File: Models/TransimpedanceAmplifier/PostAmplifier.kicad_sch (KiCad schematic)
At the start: 18 parts, among them J10 Conn_01x02_Pin, J8 Conn_01x02_Pin, J9 Conn_01x02_Pin, Q1 Q_PNP, Q2 Q_NPN, U5 OP37G

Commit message: Working on filling in the last details of the schematics
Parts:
- C15, C16: footprint (none) -> TwoTerminal:CAPC0603; Cost (none) -> $0.00; RoHS Compliant (none) -> NO
- D4, D5: footprint (none) -> TwoTerminal:SOD-123; Cost (none) -> $0.00; RoHS Compliant (none) -> NO
- D6, D7: footprint (none) -> ThreeTerminal:SOT-23; Cost (none) -> $0.00; RoHS Compliant (none) -> NO
- J10, J8, J9: footprint (none) -> Connector_Custom:PinHeader_1x2; Cost (none) -> $0.00; RoHS Compliant (none) -> NO
- Q1, Q2, R12, R13, R14, R15, R16, R17, U5: Cost (none) -> $0.00; RoHS Compliant (none) -> NO

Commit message: Fixed a bug in footprint assignment
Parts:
- Q1, Q2: footprint (none) -> ThreeTerminal:SOT-23
- R12, R13, R14, R15, R16, R17: footprint (none) -> TwoTerminal:RESC0603
- U5: footprint (none) -> IC:SOIC-8
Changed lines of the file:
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@@
 			)
 		)
-		(property "Footprint" ""
+		(property "Footprint" "TwoTerminal:RESC0603"
 			(at 49.784 143.256 90)
 			(effects
@@
 			)
 		)
-		(property "Footprint" ""
+		(property "Footprint" "TwoTerminal:RESC0603"
 			(at 247.396 52.324 90)
 			(effects
@@
 			)
 		)
-		(property "Footprint" ""
+		(property "Footprint" "TwoTerminal:RESC0603"
 			(at 247.396 128.524 90)
 			(effects
@@
 			)
 		)
-		(property "Footprint" ""
+		(property "Footprint" "TwoTerminal:RESC0603"
 			(at 202.184 136.144 90)
 			(effects
@@
 			)
 		)
-		(property "Footprint" ""
+		(property "Footprint" "IC:SOIC-8"
 			(at 67.31 101.6 0)
 			(effects
@@
 			)
 		)
-		(property "Footprint" ""
+		(property "Footprint" "ThreeTerminal:SOT-23"
 			(at 226.06 66.04 0)
 			(effects
@@
 			)
 		)
-		(property "Footprint" ""
+		(property "Footprint" "ThreeTerminal:SOT-23"
 			(at 226.06 116.84 0)
 			(effects
@@
 			)
 		)
-		(property "Footprint" ""
+		(property "Footprint" "TwoTerminal:RESC0603"
 			(at 202.184 44.704 90)
 			(effects
@@
 			)
 		)
-		(property "Footprint" ""
+		(property "Footprint" "TwoTerminal:RESC0603"
 			(at 75.184 125.984 90)
 			(effects

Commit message: Save progress
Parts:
- C15, C16: Cost $0.00 -> $0.15; Cost (qty10) (none) -> $0.087; RoHS Compliant NO -> YES
- D4, D5: Cost $0.00 -> $0.12; Cost (qty10) (none) -> $0.066; RoHS Compliant NO -> YES
- D6, D7: Cost $0.00 -> $0.78; Cost (qty10) (none) -> $0.558; RoHS Compliant NO -> YES
- J10, J8, J9: Cost $0.00 -> $0.10; Cost (qty10) (none) -> $0.025; RoHS Compliant NO -> YES
- Q1: Cost $0.00 -> $0.15; Cost (qty10) (none) -> $0.089; RoHS Compliant NO -> YES
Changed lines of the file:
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@@
 			)
 		)
-		(property "Cost" "$0.00"
+		(property "Cost" "$0.78"
 			(at 246.38 74.93 0)
 			(effects
@@
 			)
 		)
-		(property "RoHS Compliant" "NO"
+		(property "RoHS Compliant" "YES"
+			(at 246.38 74.93 0)
+			(effects
+				(font
+					(size 1.27 1.27)
+				)
+				(hide yes)
+			)
+		)
+		(property "Cost (qty10)" "$0.558"
 			(at 246.38 74.93 0)
 			(effects
@@
 			)
 		)
-		(property "Cost" "$0.00"
+		(property "Cost" "$0.10"
 			(at 55.88 43.18 0)
 			(effects
@@
 			)
 		)
-		(property "RoHS Compliant" "NO"
+		(property "RoHS Compliant" "YES"
+			(at 55.88 43.18 0)
+			(effects
+				(font
+					(size 1.27 1.27)
+				)
+				(hide yes)
+			)
+		)
+		(property "Cost (qty10)" "$0.025"
 			(at 55.88 43.18 0)
 			(effects
@@
 			)
 		)
-		(property "Cost" "$0.00"
+		(property "Cost" "$0.15"
 			(at 50.8 57.15 0)
 			(effects
@@
 			)
 		)
-		(property "RoHS Compliant" "NO"
+		(property "RoHS Compliant" "YES"
+			(at 50.8 57.15 0)
+			(effects
+				(font
+					(size 1.27 1.27)
+				)
+				(hide yes)
+			)
+		)
+		(property "Cost (qty10)" "$0.087"
 			(at 50.8 57.15 0)
 			(effects
@@
 			)
 		)
-		(property "Cost" "$0.00"
+		(property "Cost" "$0.12"
 			(at 214.63 45.72 0)
 			(effects
@@
 			)
 		)
-		(property "RoHS Compliant" "NO"
+		(property "RoHS Compliant" "YES"
+			(at 214.63 45.72 0)
+			(effects
+				(font
+					(size 1.27 1.27)
+				)
+				(hide yes)
+			)
+		)
+		(property "Cost (qty10)" "$0.066"
 			(at 214.63 45.72 0)
 			(effects
@@
 			)
 		)
-		(property "Cost" "$0.00"
+		(property "Cost" "$0.10"
 			(at 76.2 134.62 90)
 			(effects
@@
 			)
 		)
-		(property "RoHS Compliant" "NO"
+		(property "RoHS Compliant" "YES"
+			(at 76.2 134.62 90)
+			(effects
+				(font
+					(size 1.27 1.27)
+				)
+				(hide yes)
+			)
+		)
+		(property "Cost (qty10)" "$0.025"
 			(at 76.2 134.62 90)
 			(effects
@@
 			)
 		)
-		(property "Cost" "$0.00"
+		(property "Cost" "$0.15"
 			(at 226.06 66.04 0)
 			(effects
@@
 			)
 		)
-		(property "RoHS Compliant" "NO"
+		(property "RoHS Compliant" "YES"
+			(at 226.06 66.04 0)
+			(effects
+				(font
+					(size 1.27 1.27)
+				)
+				(hide yes)
+			)
+		)
+		(property "Cost (qty10)" "$0.089"
 			(at 226.06 66.04 0)
 			(effects
@@
 			)
 		)
-		(property "Cost" "$0.00"
+		(property "Cost" "$0.10"
 			(at 99.06 43.18 0)
 			(effects
@@
 			)
 		)
-		(property "RoHS Compliant" "NO"
+		(property "RoHS Compliant" "YES"
+			(at 99.06 43.18 0)
+			(effects
+				(font
+					(size 1.27 1.27)
+				)
+				(hide yes)
+			)
+		)
+		(property "Cost (qty10)" "$0.025"
 			(at 99.06 43.18 0)
 			(effects
@@
 			)
 		)
-		(property "Cost" "$0.00"
+		(property "Cost" "$0.12"
 			(at 214.63 137.16 0)
 			(effects
@@
 			)
 		)
-		(property "RoHS Compliant" "NO"
+		(property "RoHS Compliant" "YES"
+			(at 214.63 137.16 0)
+			(effects
+				(font
+					(size 1.27 1.27)
+				)
+				(hide yes)
+			)
+		)
+		(property "Cost (qty10)" "$0.066"
 			(at 214.63 137.16 0)
 			(effects
@@
 			)
 		)
-		(property "Cost" "$0.00"
+		(property "Cost" "$0.15"
 			(at 93.98 57.15 0)
 			(effects
@@
 			)
 		)
-		(property "RoHS Compliant" "NO"
+		(property "RoHS Compliant" "YES"
+			(at 93.98 57.15 0)
+			(effects
+				(font
+					(size 1.27 1.27)
+				)
+				(hide yes)
+			)
+		)
+		(property "Cost (qty10)" "$0.087"
 			(at 93.98 57.15 0)
 			(effects
@@
 			)
 		)
-		(property "Cost" "$0.00"
+		(property "Cost" "$0.78"
 			(at 246.38 100.33 0)
 			(effects
@@
 			)
 		)
-		(property "RoHS Compliant" "NO"
+		(property "RoHS Compliant" "YES"
 			(at 246.38 100.33 0)
 			(effects
+				(font
+					(size 1.27 1.27)
+				)
+				(hide yes)
+			)
+		)
+		(property "Cost (qty10)" "$0.558"
+			(at 246.38 100.33 0)
+			(effects

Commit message: Added important links regarding high-voltage electronics
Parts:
- Q2: Cost $0.00 -> $0.14; Cost (qty10) (none) -> $0.088; RoHS Compliant NO -> YES
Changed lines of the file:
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@@
 			)
 		)
-		(property "Cost" "$0.00"
+		(property "Cost" "$0.14"
 			(at 226.06 116.84 0)
 			(effects
@@
 			)
 		)
-		(property "RoHS Compliant" "NO"
+		(property "RoHS Compliant" "YES"
 			(at 226.06 116.84 0)
 			(effects
+				(font
+					(size 1.27 1.27)
+				)
+				(hide yes)
+			)
+		)
+		(property "Cost (qty10)" "$0.088"
+			(at 226.06 116.84 0)
+			(effects

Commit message: Almost done with generating bill of materials
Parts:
- R12, R14, R15: Cost $0.00 -> $0.10; Cost (qty10) (none) -> $0.030; RoHS Compliant NO -> YES
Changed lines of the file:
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@@
 			)
 		)
-		(property "Cost" "$0.00"
+		(property "Cost" "$0.10"
 			(at 50.8 143.51 0)
 			(effects
@@
 			)
 		)
-		(property "RoHS Compliant" "NO"
+		(property "RoHS Compliant" "YES"
+			(at 50.8 143.51 0)
+			(effects
+				(font
+					(size 1.27 1.27)
+				)
+				(hide yes)
+			)
+		)
+		(property "Cost (qty10)" "$0.030"
 			(at 50.8 143.51 0)
 			(effects
@@
 			)
 		)
-		(property "Cost" "$0.00"
+		(property "Cost" "$0.10"
 			(at 201.93 137.16 90)
 			(effects
@@
 			)
 		)
-		(property "RoHS Compliant" "NO"
+		(property "RoHS Compliant" "YES"
+			(at 201.93 137.16 90)
+			(effects
+				(font
+					(size 1.27 1.27)
+				)
+				(hide yes)
+			)
+		)
+		(property "Cost (qty10)" "$0.030"
 			(at 201.93 137.16 90)
 			(effects
@@
 			)
 		)
-		(property "Cost" "$0.00"
+		(property "Cost" "$0.10"
 			(at 201.93 45.72 90)
 			(effects
@@
 			)
 		)
-		(property "RoHS Compliant" "NO"
+		(property "RoHS Compliant" "YES"
 			(at 201.93 45.72 90)
 			(effects
+				(font
+					(size 1.27 1.27)
+				)
+				(hide yes)
+			)
+		)
+		(property "Cost (qty10)" "$0.030"
+			(at 201.93 45.72 90)
+			(effects

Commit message: Going to shift all the expensive, hard-to-find ICs over to Mouser
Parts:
- R13, R16, R17: Cost $0.00 -> $0.10; Cost (qty10) (none) -> $0.030; RoHS Compliant NO -> YES
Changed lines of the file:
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@@
 			)
 		)
-		(property "Cost" "$0.00"
+		(property "Cost" "$0.10"
 			(at 246.38 52.07 0)
 			(effects
@@
 			)
 		)
-		(property "RoHS Compliant" "NO"
+		(property "RoHS Compliant" "YES"
+			(at 246.38 52.07 0)
+			(effects
+				(font
+					(size 1.27 1.27)
+				)
+				(hide yes)
+			)
+		)
+		(property "Cost (qty10)" "$0.030"
 			(at 246.38 52.07 0)
 			(effects
@@
 			)
 		)
-		(property "Cost" "$0.00"
+		(property "Cost" "$0.10"
 			(at 246.38 128.27 0)
 			(effects
@@
 			)
 		)
-		(property "RoHS Compliant" "NO"
+		(property "RoHS Compliant" "YES"
+			(at 246.38 128.27 0)
+			(effects
+				(font
+					(size 1.27 1.27)
+				)
+				(hide yes)
+			)
+		)
+		(property "Cost (qty10)" "$0.030"
 			(at 246.38 128.27 0)
 			(effects
@@
 			)
 		)
-		(property "Cost" "$0.00"
+		(property "Cost" "$0.10"
 			(at 74.93 127 90)
 			(effects
@@
 			)
 		)
-		(property "RoHS Compliant" "NO"
+		(property "RoHS Compliant" "YES"
 			(at 74.93 127 90)
 			(effects
+				(font
+					(size 1.27 1.27)
+				)
+				(hide yes)
+			)
+		)
+		(property "Cost (qty10)" "$0.030"
+			(at 74.93 127 90)
+			(effects

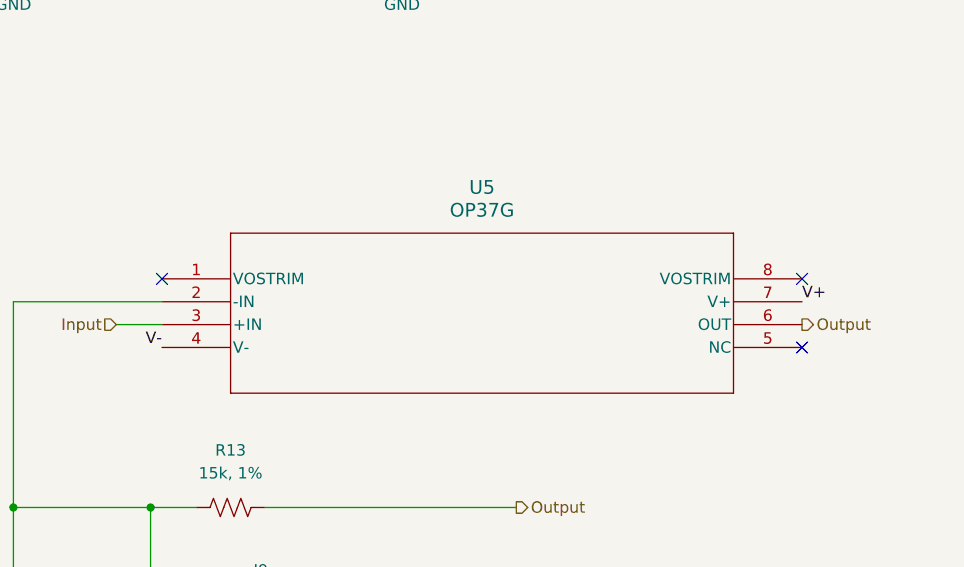
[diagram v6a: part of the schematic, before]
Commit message: Starting major changes in response to the SOIC-8 version of OP37 being out of stock
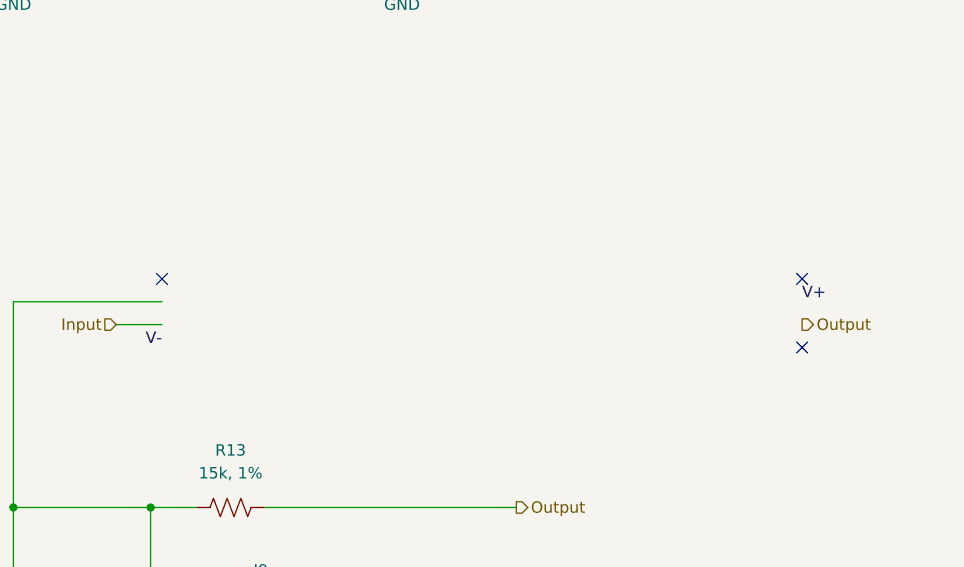
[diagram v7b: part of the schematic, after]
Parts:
- removed U5: OP37G, IC:SOIC-8, symbol OP37G:OP37GSZ
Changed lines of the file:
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@@
-	)
-	(symbol
-		(lib_id "OP37G:OP37GSZ")
-		(at 67.31 101.6 0)
-		(unit 1)
-		(exclude_from_sim no)
-		(in_bom yes)
-		(on_board yes)
-		(dnp no)
-		(fields_autoplaced yes)
-		(property "Reference" "U5"
-			(at 102.87 91.44 0)
-			(effects
-				(font
-					(size 1.524 1.524)
-				)
-			)
-		)
-		(property "Value" "OP37G"
-			(at 102.87 93.98 0)
-			(effects
-				(font
-					(size 1.524 1.524)
-				)
-			)
-		)
-		(property "Footprint" "IC:SOIC-8"
-			(at 67.31 101.6 0)
-			(effects
-				(font
-					(size 1.27 1.27)
-					(italic yes)
-				)
-				(hide yes)
-			)
-		)
-		(property "Datasheet" "https://www.analog.com/media/en/technical-documentation/data-sheets/OP37.pdf"
-			(at 67.31 101.6 0)
-			(effects
-				(font
-					(size 1.27 1.27)
-					(italic yes)
-				)
-				(hide yes)
-			)
-		)
-		(property "Description" ""
-			(at 67.31 101.6 0)
-			(effects
-				(font
-					(size 1.27 1.27)
-				)
-				(hide yes)
-			)
-		)
-		(property "Purchase Link" "https://www.mouser.com/ProductDetail/Analog-Devices/OP37GSZ?qs=WIvQP4zGangnlHcCmYh5ww%3D%3D"
-			(at 67.31 101.6 0)
-			(effects
-				(font
-					(size 1.27 1.27)
-				)
-				(hide yes)
-			)
-		)
-		(property "Cost" "$0.00"
-			(at 67.31 101.6 0)
-			(effects
-				(font
-					(size 1.27 1.27)
-				)
-				(hide yes)
-			)
-		)
-		(property "RoHS Compliant" "NO"
-			(at 67.31 101.6 0)
-			(effects
-				(font
-					(size 1.27 1.27)
-				)
-				(hide yes)
-			)
-		)
-		(pin "3"
-		)
-		(pin "6"
-		)
-		(pin "4"
-		)
-		(pin "1"
-		)
-		(pin "7"
-		)
-		(pin "5"
-		)
-		(pin "2"
-		)
-		(pin "8"
-		)
-		(instances
-			(project ""
-				(path "/ec9f2ae3-e40d-40eb-9760-2b611ee8efd1/226b3d0c-9e45-4bcf-9bef-58938aee743e/1a19fcb8-2301-474b-810f-9788696a69a6"
-					(reference "U5")
-					(unit 1)
-				)
-			)
-		)
 	)
 	(symbol

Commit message: Patching up the bill of materials now
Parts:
- added U5: OP37GPZ, symbol OP37G:OP37GPZ
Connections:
- net Input: now also U5.3 (+IN)
- net Output: now also U5.6 (OUT)
- net V+: now also U5.7 (V+)
- net V-: now also U5.4 (V-)
- net at J9.2 (Pin_2), R12.2, R13.1: now also U5.2 (-IN)
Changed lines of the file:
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@@
+	)
+	(symbol
+		(lib_id "OP37G:OP37GPZ")
+		(at 67.31 101.6 0)
+		(unit 1)
+		(exclude_from_sim no)
+		(in_bom yes)
+		(on_board yes)
+		(dnp no)
+		(fields_autoplaced yes)
+		(property "Reference" "U5"
+			(at 102.87 91.44 0)
+			(effects
+				(font
+					(size 1.524 1.524)
+				)
+			)
+		)
+		(property "Value" "OP37GPZ"
+			(at 102.87 93.98 0)
+			(effects
+				(font
+					(size 1.524 1.524)
+				)
+			)
+		)
+		(property "Footprint" ""
+			(at 67.31 101.6 0)
+			(effects
+				(font
+					(size 1.27 1.27)
+					(italic yes)
+				)
+				(hide yes)
+			)
+		)
+		(property "Datasheet" "https://www.analog.com/media/en/technical-documentation/data-sheets/OP37.pdf"
+			(at 67.31 101.6 0)
+			(effects
+				(font
+					(size 1.27 1.27)
+					(italic yes)
+				)
+				(hide yes)
+			)
+		)
+		(property "Description" ""
+			(at 67.31 101.6 0)
+			(effects
+				(font
+					(size 1.27 1.27)
+				)
+				(hide yes)
+			)
+		)
+		(property "Purchase Link" ""
+			(at 67.31 101.6 0)
+			(effects
+				(font
+					(size 1.27 1.27)
+				)
+				(hide yes)
+			)
+		)
+		(pin "3"
+		)
+		(pin "5"
+		)
+		(pin "8"
+		)
+		(pin "7"
+		)
+		(pin "6"
+		)
+		(pin "1"
+		)
+		(pin "2"
+		)
+		(pin "4"
+		)
+		(instances
+			(project ""
+				(path "/ec9f2ae3-e40d-40eb-9760-2b611ee8efd1/226b3d0c-9e45-4bcf-9bef-58938aee743e/1a19fcb8-2301-474b-810f-9788696a69a6"
+					(reference "U5")
+					(unit 1)
+				)
+			)
+		)
 	)
 	(symbol
